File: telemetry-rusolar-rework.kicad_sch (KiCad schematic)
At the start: 69 parts, among them J1 USART Debug, J10 JP, J12 I2C, J13 GR2, J14 GR1, J19 Micro_SD_Card, J2 SPI, J20 USB_C_Receptacle_USB2.0_14P, J4 CAN, J8 SWD, U2 TJA1051TK-3, U3 STM32H725VETx, Y1 50MHz

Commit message: Layout parts
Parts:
- removed D4: SD-ON, LED_SMD:LED_0805_2012Metric_Pad1.15x1.40mm_HandSolder, symbol Device:LED
- removed D7: PWR, LED_SMD:LED_0805_2012Metric_Pad1.15x1.40mm_HandSolder, symbol Device:LED_Small
- removed J20: USB_C_Receptacle_USB2.0_14P, Connector_USB:USB_C_Receptacle_HRO_TYPE-C-31-M-12, symbol Connector:USB_C_Receptacle_USB2.0_14P
- removed R10, R11: 5k1, Resistor_SMD:R_0603_1608Metric_Pad0.98x0.95mm_HandSolder, symbol Device:R
- removed R12: 1k5, Resistor_SMD:R_0603_1608Metric_Pad0.98x0.95mm_HandSolder, symbol Device:R
- removed R9: 330, Resistor_SMD:R_0603_1608Metric_Pad0.98x0.95mm_HandSolder, symbol Device:R
- added C56, C58: 100n, Capacitor_SMD:C_0603_1608Metric_Pad1.08x0.95mm_HandSolder, symbol Device:C
- added C57: 1u, Capacitor_SMD:C_0805_2012Metric_Pad1.18x1.45mm_HandSolder, symbol Device:C
- added C59: 10u, Capacitor_SMD:C_0805_2012Metric_Pad1.18x1.45mm_HandSolder, symbol Device:C
- added D13, D14, D9: LSR05-TP, SamacSys_Parts:LSR05TP, symbol SamacSys_Parts:LSR05-TP
- added D8: VESD05A1-02VHG3-08, SamacSys_Parts:VESD05A102VHG308, symbol SamacSys_Parts:VESD05A1-02VHG3-08
- added J11: USB_B_Micro, Connector_USB:USB_Micro-B_Wuerth_629105150521, symbol Connector:USB_B_Micro
- J19: footprint Connector_Card:microSD_HC_Hirose_DM3D-SF -> Connector_Card:microSD_HC_Molex_47219-2001
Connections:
- net +3.3V Buck: now also J19.4 (VDD), C58.2, C59.2, D13.4 (VCC), D14.4 (VCC), D9.4 (VCC)
- net CAN2_RX: no longer J10.1 (Pin_1)
- net CAN2_TX: no longer R13.2
- net GND: now also C56.1, C57.1, C58.1, C59.1, D13.1 (GND), D14.1 (GND), D8.1 (A), D9.1 (GND), J11.5 (GND)
- net PA0: now also J14.10 (Pin_10); no longer J13.1 (Pin_1)
- net PA1: now also J14.9 (Pin_9); no longer J13.2 (Pin_2)
- net PA10: now also J13.10 (Pin_10); no longer J13.6 (Pin_6)
- net PA15: now also J13.15 (Pin_15); no longer J13.7 (Pin_7)
- net PA4: now also J14.8 (Pin_8); no longer J13.3 (Pin_3)
- net PA8: now also J13.8 (Pin_8); no longer J13.4 (Pin_4)
- net PA9: now also J13.9 (Pin_9); no longer J13.5 (Pin_5)
- net PB0: now also J14.5 (Pin_5); no longer J13.8 (Pin_8)
- net PB1: now also J14.4 (Pin_4); no longer J13.9 (Pin_9)
- net PB10: now also J14.18 (Pin_18); no longer J13.15 (Pin_15)
- net PB11: now also J14.19 (Pin_19); no longer J13.16 (Pin_16)
- net PB14: now also J14.20 (Pin_20); no longer J13.17 (Pin_17)
- net PB15: now also J13.1 (Pin_1); no longer J13.18 (Pin_18)
- net PB2: now also J14.1 (Pin_1); no longer J13.10 (Pin_10)
- net PB4: now also J13.22 (Pin_22); no longer J13.11 (Pin_11)
- net PB5: now also J13.21 (Pin_21); no longer J13.12 (Pin_12)
- net PB8: now also J14.24 (Pin_24); no longer J13.13 (Pin_13)
- net PB9: now also J14.25 (Pin_25); no longer J13.14 (Pin_14)
- net PC0: now also J14.14 (Pin_14); no longer J13.19 (Pin_19)
- net PC1: now also J14.13 (Pin_13); no longer J13.20 (Pin_20)
- net PC13: now also J14.17 (Pin_17); no longer J14.5 (Pin_5)
- net PC14: now also J14.16 (Pin_16); no longer J14.6 (Pin_6)
- net PC15: now also J14.15 (Pin_15); no longer J14.7 (Pin_7)
- net PC2_C: now also J14.12 (Pin_12); no longer J13.21 (Pin_21)
- net PC3_C: now also J14.11 (Pin_11); no longer J13.22 (Pin_22)
- net PC4: now also J14.7 (Pin_7); no longer J14.1 (Pin_1)
- net PC5: now also J14.6 (Pin_6); no longer J14.2 (Pin_2)
- net PC6: now also J13.6 (Pin_6); no longer J14.3 (Pin_3)
- net PC7: now also J13.7 (Pin_7); no longer J14.4 (Pin_4)
- net PD0: now also J13.16 (Pin_16); no longer J14.13 (Pin_13)
- net PD1: now also J13.17 (Pin_17); no longer J14.14 (Pin_14)
- net PD10: now also J13.14 (Pin_14); no longer J14.20 (Pin_20)
- net PD11: now also J13.13 (Pin_13); no longer J14.21 (Pin_21)
- net PD12: now also J13.12 (Pin_12); no longer J14.22 (Pin_22)
- net PD13: now also J13.11 (Pin_11); no longer J14.23 (Pin_23)
- net PD15: now also J13.5 (Pin_5); no longer J14.25 (Pin_25)
- net PD3: now also J13.18 (Pin_18); no longer J14.15 (Pin_15)
- net PD4: now also J13.19 (Pin_19); no longer J14.16 (Pin_16)
- net PD5: now also J13.20 (Pin_20); no longer J14.17 (Pin_17)
- net PD8: now also J13.2 (Pin_2); no longer J14.18 (Pin_18)
- net PD9: now also J13.3 (Pin_3); no longer J14.19 (Pin_19)
- net PE2: now also J14.23 (Pin_23); no longer J14.8 (Pin_8)
- net PE4: now also J14.22 (Pin_22); no longer J14.9 (Pin_9)
- net PE5: now also J14.21 (Pin_21); no longer J14.10 (Pin_10)
- net PE7: now also J14.2 (Pin_2); no longer J14.11 (Pin_11)
- net PE8: now also J14.3 (Pin_3); no longer J14.12 (Pin_12)
- net SD1_CK: now also D14.2 (I/O_1)
- net SD1_CMD: now also D14.3 (I/O_2)
- net SD1_D0: now also D9.2 (I/O_1)
- net SD1_D1: now also D9.3 (I/O_2)
- net SD1_D2: now also D13.2 (I/O_1)
- net SD1_D3: now also D13.3 (I/O_2)
- net USB_D+: now also D1.1 (K), J11.3 (D+); no longer D1.2 (K)
- net USB_D-: now also D1.2 (K), J11.2 (D-); no longer D1.1 (K)
- net VBUS: now also C56.2, C57.2, D8.2 (K), J11.1 (VBUS)
- net CAN_N: now reaches J4.1 (Pin_1), U2.6 (CANL)
- net CAN_N: now also J10.1 (Pin_1)
- net CAN_P: now reaches J4.2 (Pin_2), U2.7 (CANH)
- net CAN_P: now also R13.2
- net PD14 renamed PD14*
- net PD14*: now also J13.4 (Pin_4); no longer J14.24 (Pin_24)
- new net: C1.2, U3.44 (VCAP)
- new net: C3.2, U3.97 (VCAP)
- new net: C2.2, U3.72 (VCAP)
- no-connect marks 5 -> 7
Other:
- note added: "AN4879 STM32: H7 has built-in pullup resistor on D+"
- note added: "TODO: pull up resistor: no"
- moved on the sheet: D1, J10, R13

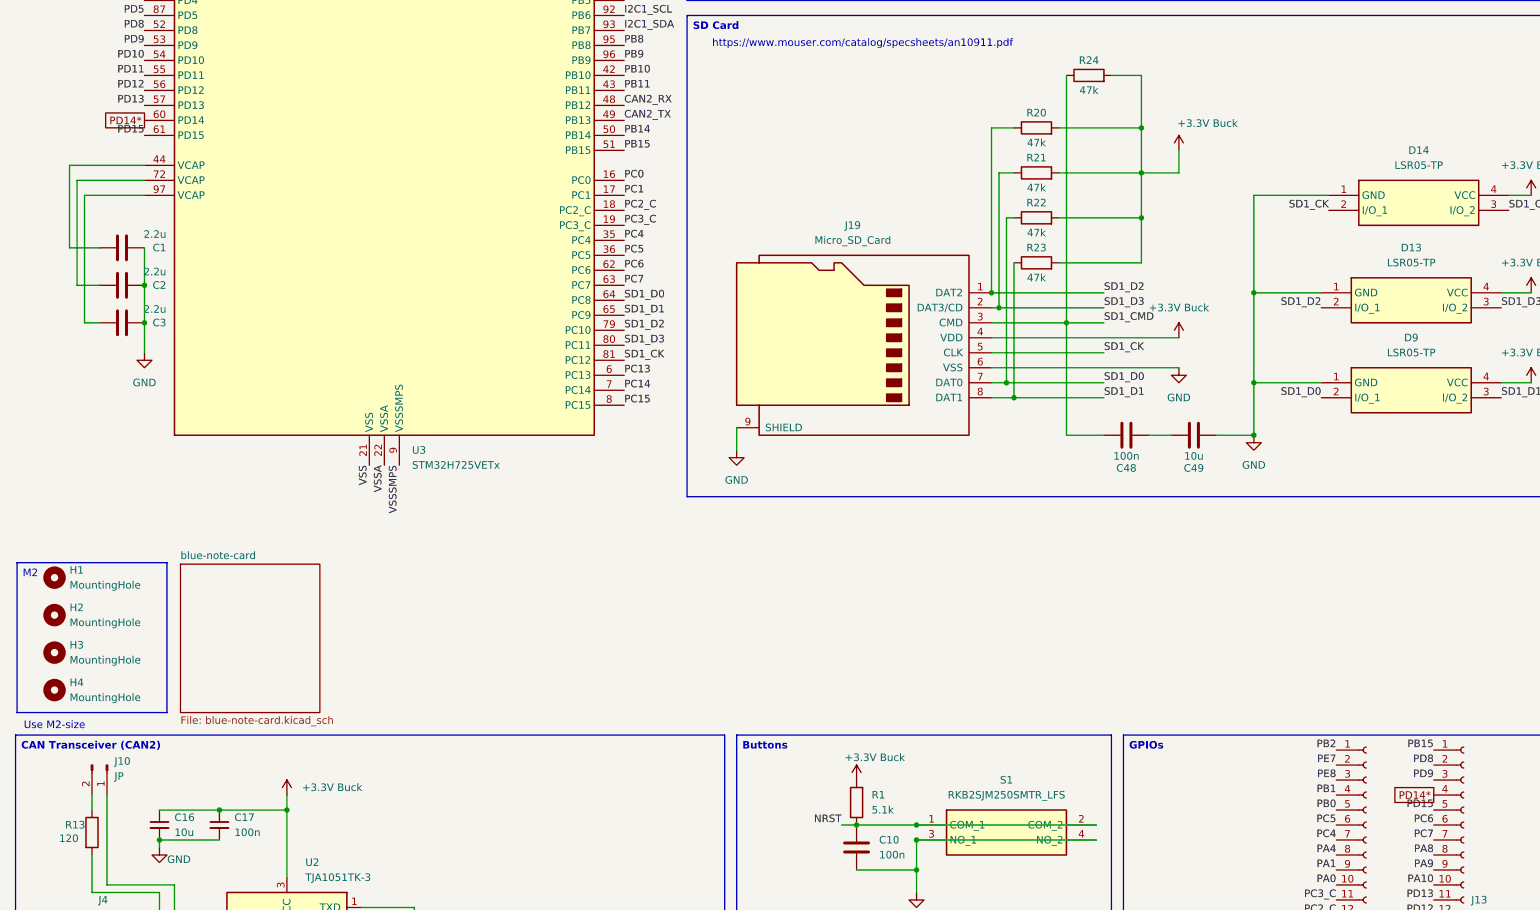
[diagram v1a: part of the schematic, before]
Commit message: Fixed DRC errors
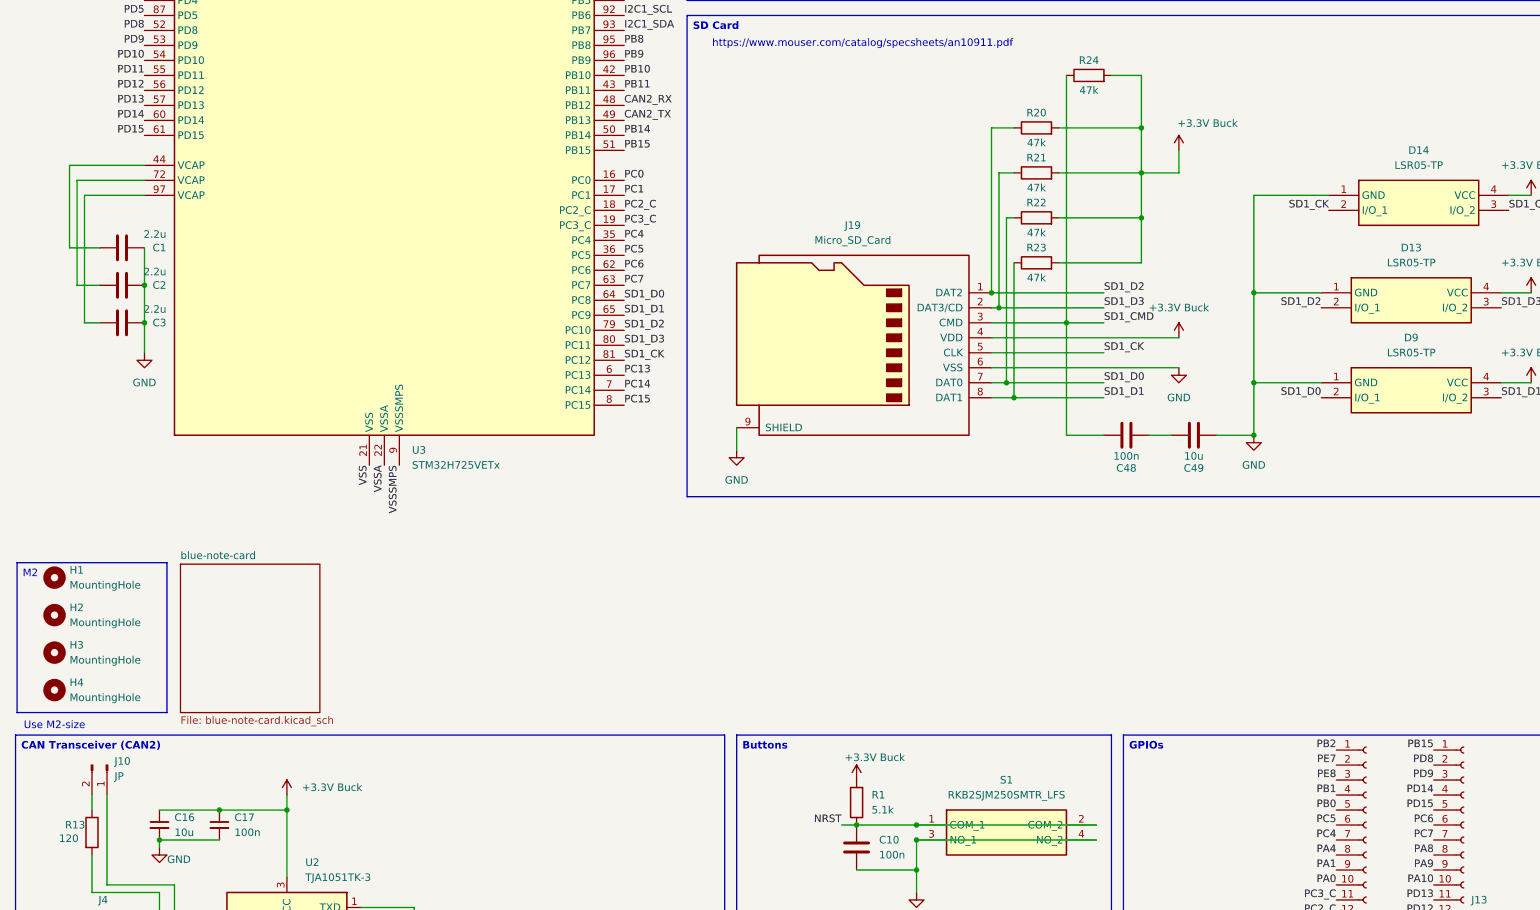
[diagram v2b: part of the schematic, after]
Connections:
- net PD14* renamed PD14

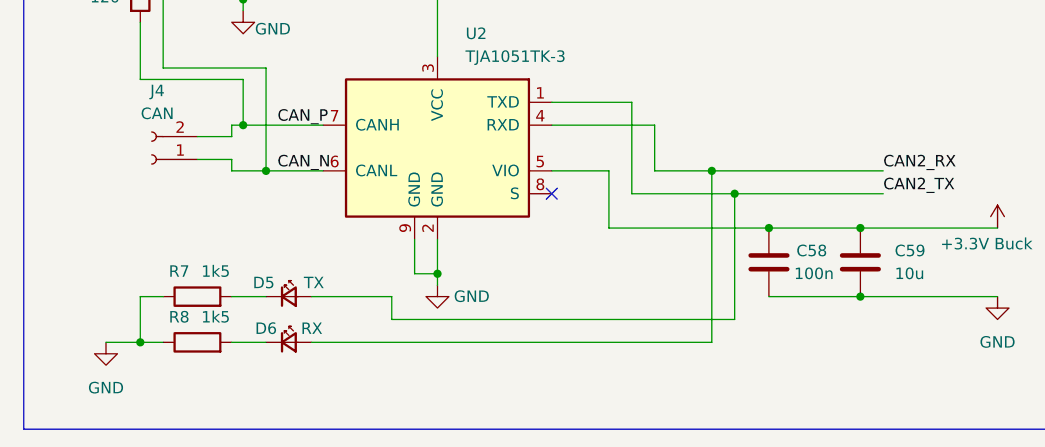
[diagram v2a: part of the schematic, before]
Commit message: Removed CAN TX/RX LED indicators
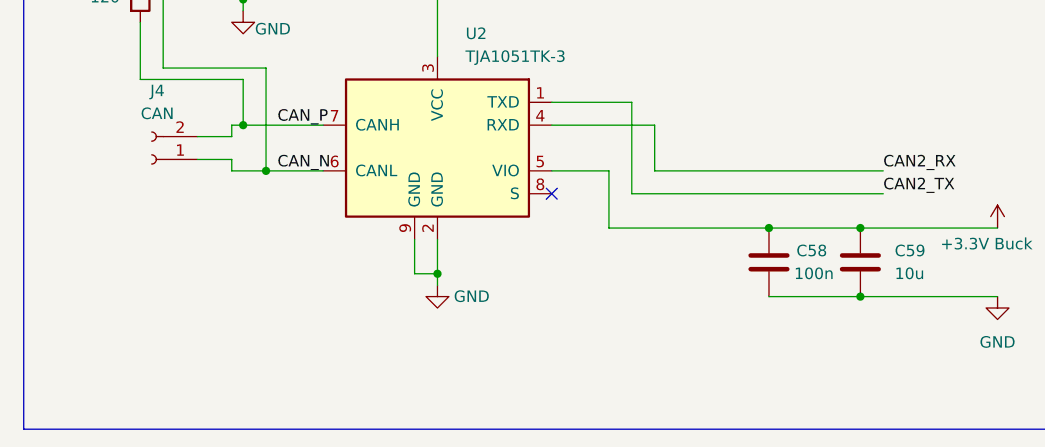
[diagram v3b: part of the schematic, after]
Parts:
- removed D5: TX, LED_SMD:LED_0805_2012Metric_Pad1.15x1.40mm_HandSolder, symbol Device:LED_Small
- removed D6: RX, LED_SMD:LED_0805_2012Metric_Pad1.15x1.40mm_HandSolder, symbol Device:LED_Small
- removed R7, R8: 1k5, Resistor_SMD:R_0805_2012Metric_Pad1.20x1.40mm_HandSolder, symbol Device:R

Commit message: Added LED indicators, USER LEDs, extended layout, fixed footprints
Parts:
- removed J19: Micro_SD_Card, Connector_Card:microSD_HC_Molex_47219-2001, symbol Connector:Micro_SD_Card
- added C62: 100n, Capacitor_SMD:C_0603_1608Metric_Pad1.08x0.95mm_HandSolder, symbol Device:C_Small
- added D15: CAN_ERR, LED_SMD:LED_0805_2012Metric_Pad1.15x1.40mm_HandSolder, symbol Device:LED
- added D16: USER LED 1, LED_SMD:LED_0805_2012Metric_Pad1.15x1.40mm_HandSolder, symbol Device:LED
- added D17: USER LED 2, LED_SMD:LED_0805_2012Metric_Pad1.15x1.40mm_HandSolder, symbol Device:LED
- added D5: CAN_PWR, LED_SMD:LED_0805_2012Metric_Pad1.15x1.40mm_HandSolder, symbol Device:LED
- added D6: TX, LED_SMD:LED_0805_2012Metric_Pad1.15x1.40mm_HandSolder, symbol Device:LED
- added D7: RX, LED_SMD:LED_0805_2012Metric_Pad1.15x1.40mm_HandSolder, symbol Device:LED
- added FB1: FerriteBead, Inductor_SMD:L_0805_2012Metric_Pad1.05x1.20mm_HandSolder, symbol Device:FerriteBead
- added J16: 47219-2001, SamacSys_Parts:472192001, symbol SamacSys_Parts:47219-2001
- added R32, R33, R34, R35, R7, R8: 1k5, Resistor_SMD:R_0603_1608Metric_Pad0.98x0.95mm_HandSolder, symbol Device:R_Small
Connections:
- net +3.3V Buck: now also J16.4 (VDD), R7.1
- net GND: now also C62.2, D15.1 (K), D16.1 (K), D17.1 (K), D5.1 (K), D6.1 (K), D7.1 (K), FB1.1, J16.10 (GND_2), J16.11 (GND_3), J16.12 (GND_4), J16.6 (VSS), J16.9 (GND_1)
- net SD1_CK: now also J16.5 (CLK)
- net SD1_CMD: now also J16.3 (CMD)
- net SD1_D0: now also J16.7 (DAT0)
- net SD1_D1: now also J16.8 (DAT1)
- net SD1_D2: now also J16.1 (DAT2)
- net SD1_D3: now also J16.2 (CD/DAT3)
- net at J11.6 (Shield): now also C62.1, FB1.2
- net PA4 renamed PA4*
- net PA4*: now also R33.1
- net PB1 renamed PB1*
- net PB1*: now also R8.1
- net PB2 renamed PB2*
- net PB2*: now also R32.1
- net PB5 renamed PB5*
- net PB5*: now also R35.1
- net PE2 renamed PE2*
- net PE2*: now also R34.1
- new net: D17.2 (A), R35.2
- new net: D5.2 (A), R7.2
- new net: D16.2 (A), R34.2
- new net: D6.2 (A), R8.2
- new net: D7.2 (A), R32.2
- new net: D15.2 (A), R33.2
- no-connect marks 7 -> 6
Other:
- note added: "GREEN"
- note added: "RED"
- note added: "YELLOW"

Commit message: Added changes
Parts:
- C47: footprint Capacitor_SMD:C_0805_2012Metric_Pad1.18x1.45mm_HandSolder -> Capacitor_SMD:C_0603_1608Metric_Pad1.08x0.95mm_HandSolder
- J1, J12: footprint Connector_PinSocket_2.00mm:PinSocket_1x02_P2.00mm_Vertical -> Connector_PinHeader_2.00mm:PinHeader_1x02_P2.00mm_Vertical
- J2: footprint Connector_PinSocket_2.00mm:PinSocket_1x03_P2.00mm_Vertical -> Connector_PinHeader_2.00mm:PinHeader_1x03_P2.00mm_Vertical

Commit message: Fixed USB VSENSE, fixed things
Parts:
- removed C62: 100n, Capacitor_SMD:C_0603_1608Metric_Pad1.08x0.95mm_HandSolder, symbol Device:C_Small
- removed D1: PESD2USB3UV, Package_TO_SOT_SMD:SOT-23W, symbol Device:D_Zener_Dual_CommonAnode_KKA
- removed D8: VESD05A1-02VHG3-08, SamacSys_Parts:VESD05A102VHG308, symbol SamacSys_Parts:VESD05A1-02VHG3-08
- removed FB1: FerriteBead, Inductor_SMD:L_0805_2012Metric_Pad1.05x1.20mm_HandSolder, symbol Device:FerriteBead
- removed J4: CAN, Connector_PinSocket_2.00mm:PinSocket_1x02_P2.00mm_Vertical, symbol Connector:Conn_01x02_Socket
- added C63: 100n, Capacitor_SMD:C_0603_1608Metric_Pad1.08x0.95mm_HandSolder, symbol Device:C
- added D2: ESDA7P60-1U1M, SamacSys_Parts:ESDA7P601U1M, symbol SamacSys_Parts:ESDA7P60-1U1M
- added F2: Fuse, Fuse:Fuse_0603_1608Metric_Pad1.05x0.95mm_HandSolder, symbol Device:Fuse
- added IC3: USBLC6-2P6, SamacSys_Parts:USBLC62P6, symbol SamacSys_Parts:USBLC6-2P6
- added J9: 53048-0210, SamacSys_Parts:SHDRRA2W35P0X125_1X2_425X550X350P, symbol SamacSys_Parts:53048-0210
- added R36: 33k, Resistor_SMD:R_0603_1608Metric_Pad0.98x0.95mm_HandSolder, symbol Device:R
- added R37: 82k, Resistor_SMD:R_0603_1608Metric_Pad0.98x0.95mm_HandSolder, symbol Device:R
- added R38: 10k, Resistor_SMD:R_0603_1608Metric_Pad0.98x0.95mm_HandSolder, symbol Device:R
- C56: value 100n -> 1u; footprint Capacitor_SMD:C_0603_1608Metric_Pad1.08x0.95mm_HandSolder -> Capacitor_SMD:C_0805_2012Metric_Pad1.18x1.45mm_HandSolder
- C57: value 1u -> 100n; footprint Capacitor_SMD:C_0805_2012Metric_Pad1.18x1.45mm_HandSolder -> Capacitor_SMD:C_0603_1608Metric_Pad1.08x0.95mm_HandSolder
- R34, R35: value 1k5 -> 470
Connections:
- net +3.3V Buck: no longer C16.1, C17.1, R7.1, U2.3 (VCC)
- net CAN_N: now also J9.1
- net CAN_P: now also J9.2
- net GND: now also C56.2, C57.2, C63.2, D2.2 (A), IC3.2 (GND), R37.2, R38.2; no longer C56.1, C57.1
- net USB_D+: now also IC3.1 (I/O1_1); no longer J11.3 (D+)
- net USB_D-: now also IC3.3 (I/O2_1); no longer J11.2 (D-)
- net VBUS: now also C56.1, C57.1, D2.1 (K), F2.1, IC3.5 (VBUS); no longer C56.2, C57.2
- net at U2.8 (S): now also R38.1
- net PA9: no longer names the net of J13.9 (Pin_9)
- net PA9: no longer U3.67 (PA9)
- new net: F2.2, R36.1
- new net: IC3.4 (I/O2_2), J11.2 (D-)
- new net: IC3.6 (I/O1_2), J11.3 (D+)
- new net +5V: C16.1, C17.1, R7.1, U2.3 (VCC)
- new net VSENSE_USB: C63.1, R36.2, R37.1, U3.67 (PA9)
- no-connect marks 6 -> 7
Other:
- note removed: "AN4879 STM32: H7 has built-in pullup resistor on D+"
- note removed: "TODO: pull up resistor: no"
- moved on the sheet: J11

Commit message: Fixed things
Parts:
- removed J8: SWD, SamacSys_Parts:FTSH-105-XX-YYY-DV-K-A, symbol SamacSys_Parts:FTSH-105-01-L-DV-K-A
- added J18: SWD, Connector_PinHeader_2.00mm:PinHeader_1x06_P2.00mm_Vertical, symbol Connector:Conn_01x06_Pin
- added R9: 2k2, Resistor_SMD:R_0603_1608Metric_Pad0.98x0.95mm_HandSolder, symbol Device:R_Small
- R32, R33, R8: value 1k5 -> 470
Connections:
- net +3.3V Buck: now also J18.1 (Pin_1)
- net GND: now also J18.2 (Pin_2)
- net NRST: now also J18.6 (Pin_6)
- net PB10: now also R9.1; no longer J14.18 (Pin_18)
- net SWD_CLK: now also J18.4 (Pin_4)
- net SWD_IO: now also J18.3 (Pin_3)
- net SWO: now also J18.5 (Pin_5)
- net +5V renamed +5V Buck
- new net PB10_PIN_HEADER: J14.18 (Pin_18), R9.2
- no-connect marks 7 -> 5
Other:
- added sheet ESP32-Wifi (esp32.kicad_sch)

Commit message: Fixed a lot of things
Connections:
- net GND: now also J11.6 (Shield)
- no-connect marks 5 -> 4
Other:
- note added: "UART4 RX"
- note added: "UART4 TX"
